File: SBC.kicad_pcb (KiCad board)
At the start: 4 copper layers, 0.6 x 0.9 mm, 128 parts, among them J1 MSD-1-A, J2 RJ45_Amphenol_RJMG1BD3B8K1ANR, J3 DX07S016JA1R1500, U1 MIC5501-3.0YM5, U10 USBLC6-2SC6, U11 USBLC6-2SC6, U12 USBLC6-2SC6, U2 TLV62569DBV, U3 TLV62569DBV, U4 TLV62569DBV, U5 Allwinner_V3s, U6 USBLC6-2SC6, U7 USBLC6-2SC6, U8 USBLC6-2SC6, U9 USBLC6-2SC6, Y1 Crystal

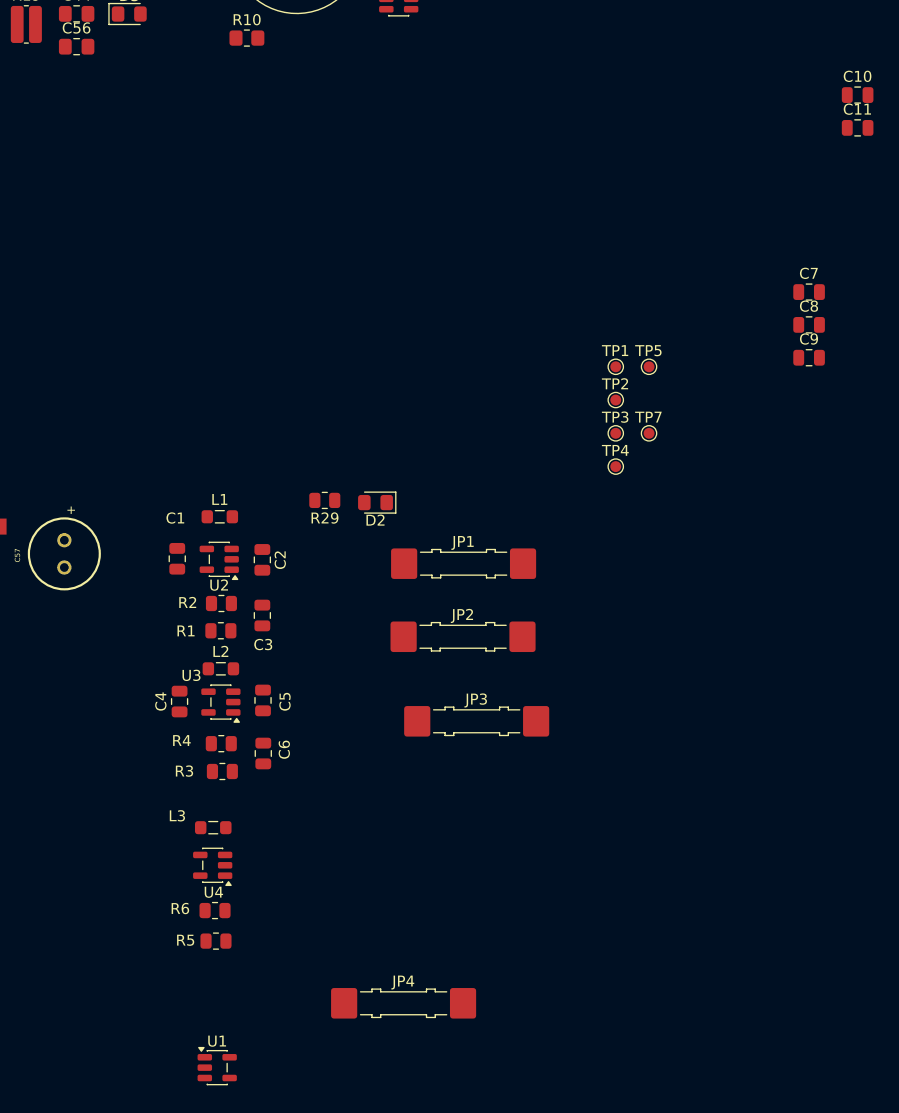
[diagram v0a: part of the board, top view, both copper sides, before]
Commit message: sorted power in pcb
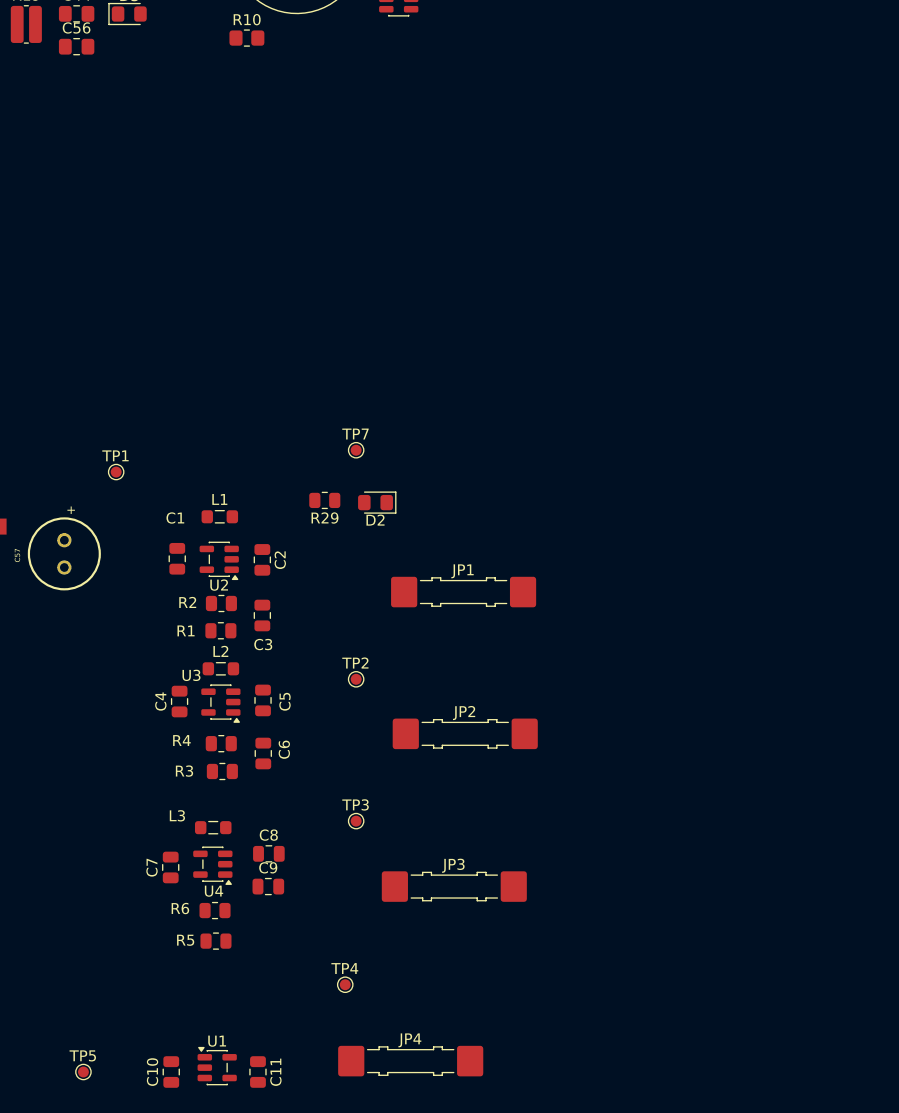
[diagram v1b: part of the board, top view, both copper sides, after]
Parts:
- moved C10 109.5 mm to (64.0, 169.0), turned to 90 degrees
- moved C11 102.5 mm to (72.0, 169.0), turned to -90 degrees
- moved TP5 82.9 mm to (56.0, 169.0)
- moved C7 78.8 mm to (64.0, 150.2), turned to 90 degrees
- moved C9 69.3 mm to (73.0, 152.0)
- moved C8 69.3 mm to (73.0, 149.0)
- moved TP4 53.6 mm to (80.0, 161.0)
- moved TP1 46.8 mm to (59.0, 114.0)
- moved TP3 42.8 mm to (81.0, 146.0)
- moved TP2 35.0 mm to (81.0, 133.0)
- moved TP7 26.9 mm to (81.0, 112.0)
- moved JP3 15.3 mm to (90.0, 152.0)
- moved JP2 8.90 mm to (91.0, 138.0)
- moved JP4 5.34 mm to (86.0, 168.0)
- moved JP1 2.60 mm to (90.8, 125.0)
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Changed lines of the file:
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@@
 	(footprint "Capacitor_SMD:C_0805_2012Metric"
 		(layer "F.Cu")
-		(at 126.9725 82.45)
+		(at 72 169 -90)
 		(descr "Capacitor SMD 0805 (2012 Metric), square (rectangular) end terminal, IPC-7351 nominal, (Body size source: IPC-SM-782 page 76, https://www.pcb-3d.com/wordpress/wp-content/uploads/ipc-sm-782a_amendment_1_and_2.pdf, https://docs.google.com/spreadsheets/d/1BsfQQcO9C6DZCsRaXUlFlo91Tg2WpOkGARC1WS5S8t0/edit?usp=sharing)")
 		(tags "capacitor")
 		(property "Reference" "C11"
-			(at 0 -1.68 0)
+			(at 0 -1.68 90)
 			(layer "F.SilkS")
 			(effects
@@
 		)
 		(property "Value" "1uF"
-			(at 0 1.68 0)
+			(at 0 1.68 90)
 			(layer "F.Fab")
 			(effects
@@
 		)
 		(property "Datasheet" ""
-			(at 0 0 0)
+			(at 0 0 90)
 			(layer "F.Fab")
 			(hide yes)
@@
 		)
 		(property "Description" "Unpolarized capacitor"
-			(at 0 0 0)
+			(at 0 0 90)
 			(layer "F.Fab")
 			(hide yes)
@@
 		)
 		(property "KiLib_Generator" "SMD_2terminal_chip_molded"
-			(at 0 0 0)
+			(at 0 0 90)
 			(layer "F.SilkS")
 			(hide yes)
@@
 		(duplicate_pad_numbers_are_jumpers no)
 		(fp_line
-			(start -0.261252 -0.735)
-			(end 0.261252 -0.735)
+			(start -0.261252 0.735)
+			(end 0.261252 0.735)
 			(stroke
 				(width 0.12)
@@
 		)
 		(fp_line
-			(start -0.261252 0.735)
-			(end 0.261252 0.735)
+			(start -0.261252 -0.735)
+			(end 0.261252 -0.735)
 			(stroke
 				(width 0.12)
@@
 		)
 		(fp_text user "${REFERENCE}"
-			(at 0 0 0)
+			(at 0 0 90)
 			(layer "F.Fab")
 			(effects
@@
 		)
 		(pad "1" smd roundrect
-			(at -0.95 0)
+			(at -0.95 0 270)
 			(size 1 1.45)
 			(layers "F.Cu" "F.Mask" "F.Paste")
@@
 		)
 		(pad "2" smd roundrect
-			(at 0.95 0)
+			(at 0.95 0 270)
 			(size 1 1.45)
 			(layers "F.Cu" "F.Mask" "F.Paste")
@@
 	(footprint "TestPoint:TestPoint_Pad_D1.0mm"
 		(layer "F.Cu")
-		(at 107.85 110.45)
+		(at 81 112)
 		(descr "SMD pad as test Point, diameter 1.0mm")
 		(tags "test point SMD pad")
@@
 	(footprint "TestPoint:TestPoint_Pad_D1.0mm"
 		(layer "F.Cu")
-		(at 104.8 110.45)
+		(at 81 146)
 		(descr "SMD pad as test Point, diameter 1.0mm")
 		(tags "test point SMD pad")
@@
 	(footprint "Package_TO_SOT_SMD:SOT-23-5"
 		(layer "F.Cu")
-		(at 67.85 150.05 180)
+		(at 67.8625 149.95 180)
 		(descr "SOT, 5 Pin (JEDEC MO-178 Var AA https://www.jedec.org/document_search?search_api_views_fulltext=MO-178)")
 		(tags "SOT TO_SOT_SMD")
@@
 	(footprint "Capacitor_SMD:C_0805_2012Metric"
 		(layer "F.Cu")
-		(at 122.5225 97.5)
+		(at 64 150.25 90)
 		(descr "Capacitor SMD 0805 (2012 Metric), square (rectangular) end terminal, IPC-7351 nominal, (Body size source: IPC-SM-782 page 76, https://www.pcb-3d.com/wordpress/wp-content/uploads/ipc-sm-782a_amendment_1_and_2.pdf, https://docs.google.com/spreadsheets/d/1BsfQQcO9C6DZCsRaXUlFlo91Tg2WpOkGARC1WS5S8t0/edit?usp=sharing)")
 		(tags "capacitor")
 		(property "Reference" "C7"
-			(at 0 -1.68 0)
+			(at 0 -1.68 90)
 			(layer "F.SilkS")
 			(effects
@@
 		)
 		(property "Value" "4.7uF"
-			(at 0 1.68 0)
+			(at 0 1.68 90)
 			(layer "F.Fab")
 			(effects
@@
 		)
 		(property "Datasheet" ""
-			(at 0 0 0)
+			(at 0 0 90)
 			(layer "F.Fab")
 			(hide yes)
@@
 		)
 		(property "Description" "Unpolarized capacitor"
-			(at 0 0 0)
+			(at 0 0 90)
 			(layer "F.Fab")
 			(hide yes)
@@
 		)
 		(property "KiLib_Generator" "SMD_2terminal_chip_molded"
-			(at 0 0 0)
+			(at 0 0 90)
 			(layer "F.SilkS")
 			(hide yes)
@@
 		)
 		(fp_text user "${REFERENCE}"
-			(at 0 0 0)
+			(at 0 0 90)
 			(layer "F.Fab")
 			(effects
@@
 		)
 		(pad "1" smd roundrect
-			(at -0.95 0)
+			(at -0.95 0 90)
 			(size 1 1.45)
 			(layers "F.Cu" "F.Mask" "F.Paste")
@@
 		)
 		(pad "2" smd roundrect
-			(at 0.95 0)
+			(at 0.95 0 90)
 			(size 1 1.45)
 			(layers "F.Cu" "F.Mask" "F.Paste")
@@
 	(footprint "TestPoint:TestPoint_Pad_D1.0mm"
 		(layer "F.Cu")
-		(at 107.85 104.35)
+		(at 56 169)
 		(descr "SMD pad as test Point, diameter 1.0mm")
 		(tags "test point SMD pad")
@@
 	(footprint "Jumper:Jumper_Harwin_S1621_P10.9mm"
 		(layer "F.Cu")
-		(at 85.35 162.7)
+		(at 86 168)
 		(descr "Harwin SMD jumper link, 12.3x2.3mm, 1.8mm height, 10.9mm pad pitch, https://cdn.harwin.com/pdfs/S1621R.pdf")
 		(tags "SMD jumper link")
@@
 	(footprint "TestPoint:TestPoint_Pad_D1.0mm"
 		(layer "F.Cu")
-		(at 104.8 104.35)
+		(at 59 114)
 		(descr "SMD pad as test Point, diameter 1.0mm")
 		(tags "test point SMD pad")
@@
 	(footprint "Capacitor_SMD:C_0805_2012Metric"
 		(layer "F.Cu")
-		(at 122.5225 103.52)
+		(at 72.95 152)
 		(descr "Capacitor SMD 0805 (2012 Metric), square (rectangular) end terminal, IPC-7351 nominal, (Body size source: IPC-SM-782 page 76, https://www.pcb-3d.com/wordpress/wp-content/uploads/ipc-sm-782a_amendment_1_and_2.pdf, https://docs.google.com/spreadsheets/d/1BsfQQcO9C6DZCsRaXUlFlo91Tg2WpOkGARC1WS5S8t0/edit?usp=sharing)")
 		(tags "capacitor")
@@
 	(footprint "Jumper:Jumper_Harwin_S1621_P10.9mm"
 		(layer "F.Cu")
-		(at 92.05 136.85)
+		(at 90 152)
 		(descr "Harwin SMD jumper link, 12.3x2.3mm, 1.8mm height, 10.9mm pad pitch, https://cdn.harwin.com/pdfs/S1621R.pdf")
 		(tags "SMD jumper link")
@@
 	(footprint "Jumper:Jumper_Harwin_S1621_P10.9mm"
 		(layer "F.Cu")
-		(at 90.8 129.1)
+		(at 91 138)
 		(descr "Harwin SMD jumper link, 12.3x2.3mm, 1.8mm height, 10.9mm pad pitch, https://cdn.harwin.com/pdfs/S1621R.pdf")
 		(tags "SMD jumper link")
@@
 	(footprint "TestPoint:TestPoint_Pad_D1.0mm"
 		(layer "F.Cu")
-		(at 104.8 113.5)
+		(at 80 161)
 		(descr "SMD pad as test Point, diameter 1.0mm")
 		(tags "test point SMD pad")
@@
 	(footprint "Capacitor_SMD:C_0805_2012Metric"
 		(layer "F.Cu")
-		(at 126.9725 79.44)
+		(at 64.05 169 90)
 		(descr "Capacitor SMD 0805 (2012 Metric), square (rectangular) end terminal, IPC-7351 nominal, (Body size source: IPC-SM-782 page 76, https://www.pcb-3d.com/wordpress/wp-content/uploads/ipc-sm-782a_amendment_1_and_2.pdf, https://docs.google.com/spreadsheets/d/1BsfQQcO9C6DZCsRaXUlFlo91Tg2WpOkGARC1WS5S8t0/edit?usp=sharing)")
 		(tags "capacitor")
 		(property "Reference" "C10"
-			(at 0 -1.68 0)
+			(at 0 -1.68 90)
 			(layer "F.SilkS")
 			(effects
@@
 		)
 		(property "Value" "1uF"
-			(at 0 1.68 0)
+			(at 0 1.68 90)
 			(layer "F.Fab")
 			(effects
@@
 		)
 		(property "Datasheet" ""
-			(at 0 0 0)
+			(at 0 0 90)
 			(layer "F.Fab")
 			(hide yes)
@@
 		)
 		(property "Description" "Unpolarized capacitor"
-			(at 0 0 0)
+			(at 0 0 90)
 			(layer "F.Fab")
 			(hide yes)
@@
 		)
 		(property "KiLib_Generator" "SMD_2terminal_chip_molded"
-			(at 0 0 0)
+			(at 0 0 90)
 			(layer "F.SilkS")
 			(hide yes)
@@
 		)
 		(fp_text user "${REFERENCE}"
-			(at 0 0 0)
+			(at 0 0 90)
 			(layer "F.Fab")
 			(effects
@@
 		)
 		(pad "1" smd roundrect
-			(at -0.95 0)
+			(at -0.95 0 90)
 			(size 1 1.45)
 			(layers "F.Cu" "F.Mask" "F.Paste")
@@
 		)
 		(pad "2" smd roundrect
-			(at 0.95 0)
+			(at 0.95 0 90)
 			(size 1 1.45)
 			(layers "F.Cu" "F.Mask" "F.Paste")
@@
 	(footprint "Jumper:Jumper_Harwin_S1621_P10.9mm"
 		(layer "F.Cu")
-		(at 90.85 122.4)
+		(at 90.85 125)
 		(descr "Harwin SMD jumper link, 12.3x2.3mm, 1.8mm height, 10.9mm pad pitch, https://cdn.harwin.com/pdfs/S1621R.pdf")
 		(tags "SMD jumper link")
@@
 	(footprint "TestPoint:TestPoint_Pad_D1.0mm"
 		(layer "F.Cu")
-		(at 104.8 107.4)
+		(at 81 133)
 		(descr "SMD pad as test Point, diameter 1.0mm")
 		(tags "test point SMD pad")
@@
 	(footprint "Capacitor_SMD:C_0805_2012Metric"
 		(layer "F.Cu")
-		(at 122.5225 100.51)
+		(at 73 149)
 		(descr "Capacitor SMD 0805 (2012 Metric), square (rectangular) end terminal, IPC-7351 nominal, (Body size source: IPC-SM-782 page 76, https://www.pcb-3d.com/wordpress/wp-content/uploads/ipc-sm-782a_amendment_1_and_2.pdf, https://docs.google.com/spreadsheets/d/1BsfQQcO9C6DZCsRaXUlFlo91Tg2WpOkGARC1WS5S8t0/edit?usp=sharing)")
 		(tags "capacitor")
